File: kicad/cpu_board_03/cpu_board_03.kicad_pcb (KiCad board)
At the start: 2 copper layers, 99.1 x 94.2 mm, 60 parts, among them J1 DIN41612_02x32_AC, J10 PLD_aux, J11 Conn_01x09, J6 Conn_01x02_Socket, J9 Ram1 Enable, SW1 SW_Reset, SW2 SW_PWR, U1 W65C02SxP, U10 74HC245, U11 74HC245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

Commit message: update label names
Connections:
- net /~{CS_RAM0} renamed /~{RAM0_SEL}
- net /~{CS_RAM1} renamed /~{RAM1_SEL}
- net /~{CS_ROM} renamed /~{ROM_SEL}
- net /~{IO_RD_DIR} renamed /~{IO_RD}
- net /~{QOE} renamed /~{OE}
- net /~{QWE_RAM} renamed /~{QWE}
- net /~{SYS_CLK} renamed /~{IO_WR}

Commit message: update pcb
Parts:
- removed U14: 74AHC1G04, Package_TO_SOT_SMD:SOT-23-5_HandSoldering
- moved U13 3.14 mm to (113.5, 56.4)
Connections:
- U13 pad 1: Net-(U13-Pad1) -> /~{IO_WR}
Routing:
- net /CLOCK: track 55.8 -> 31.3 mm, vias 1 -> 0
- net Net-(U13-Pad1): track 17.4 -> 0.00 mm
- net VCC: track 546.1 -> 538.4 mm
- net /~{IO_WR}: track 51.9 -> 56.6 mm
- net Net-(U6-Cp): track 21.8 -> 18.3 mm
- net /~{IOEN_00_GPIO0}: track 112.8 -> 110.0 mm
- net GND: track 929.6 -> 928.8 mm, vias 76 -> 74

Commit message: cleaned up pullup mess
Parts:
- added D14: LED_Small, LED_SMD:LED_0805_2012Metric_Pad1.15x1.40mm_HandSolder, F.Cu at (46.5, 75.7)
- added R6: 10K, Resistor_SMD:R_0805_2012Metric_Pad1.20x1.40mm_HandSolder, F.Cu at (46.5, 73.2)
- added R7: 10K, Resistor_SMD:R_0805_2012Metric_Pad1.20x1.40mm_HandSolder, F.Cu at (46.5, 78.0)
- added R8: 10K, Resistor_SMD:R_0805_2012Metric_Pad1.20x1.40mm_HandSolder, F.Cu at (46.5, 65.5)
- moved C11 5.95 mm to (41.3, 61.2)
- moved R5 1.59 mm to (46.5, 70.6), turned to 0 degrees
- moved R3 0.55 mm to (46.5, 68.1), turned to 0 degrees
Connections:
- J1 pad a29: VCC -> /~{IRQ}
- J1 pad a30: /~{NMI} -> /BE
- J1 pad c29: GND -> /RDY
- J1 pad c30: /~{IRQ} -> /~{NMI}
- U1 pad 2: VCC -> /RDY
- U1 pad 36: VCC -> /BE
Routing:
- net /BE: track 0.00 -> 55.6 mm
- net /RDY: track 0.00 -> 34.3 mm
- net VCC: track 538.4 -> 512.2 mm, vias 4 -> 7
- net /~{IRQ}: track 41.1 -> 49.1 mm
- net /~{NMI}: track 57.6 -> 51.7 mm
- net Net-(D14-A): track 0.00 -> 2.30 mm
- net /RES: track 47.0 -> 47.9 mm
- net /~{RES}: track 74.3 -> 74.9 mm
- net GND: track 928.8 -> 928.2 mm, vias 74 -> 71
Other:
- board text added: "Rdy"

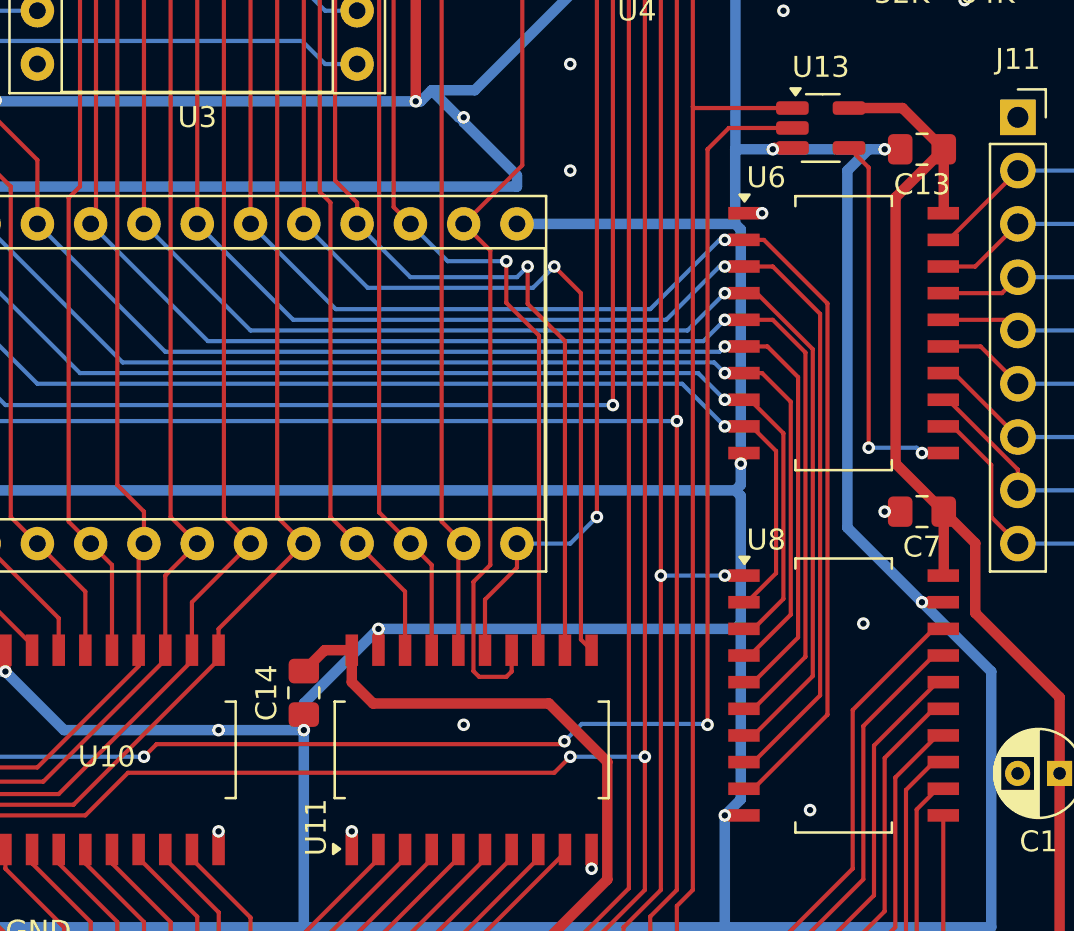
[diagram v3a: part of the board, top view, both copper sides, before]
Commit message: add bus tranceiver OE signal
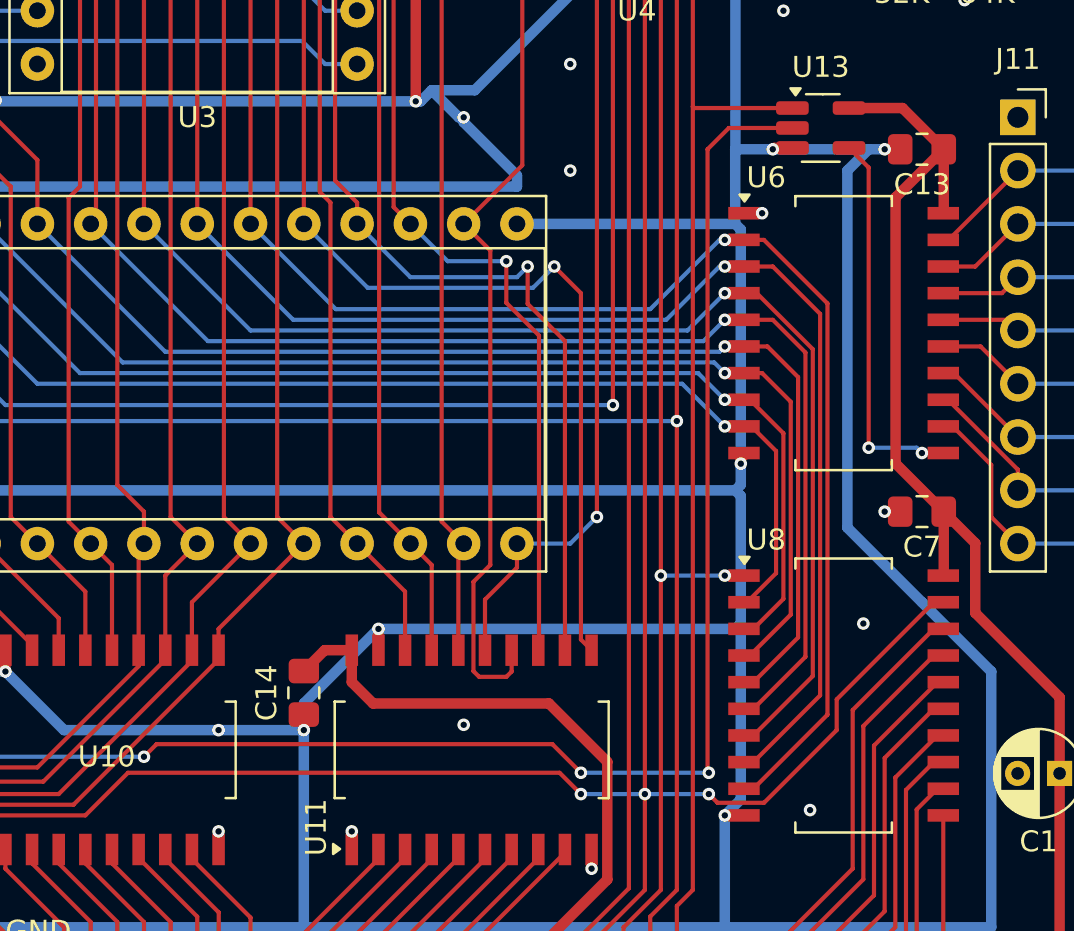
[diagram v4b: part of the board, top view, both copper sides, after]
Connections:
- U8 pad 19: GND -> /~{IO_SEL}
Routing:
- net /~{IO_SEL}: track 124.2 -> 143.5 mm, vias 5 -> 6
- net /~{IOEN_00_GPIO0}: track 110.0 -> 112.5 mm
- net GND: track 928.2 -> 927.2 mm, vias 71 -> 70
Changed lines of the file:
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@@
 			(size 1.5 0.6)
 			(layers "F.Cu" "F.Mask" "F.Paste")
-			(net 17 "GND")
+			(net 36 "/~{IO_SEL}")
 			(pinfunction "CE")
 			(pintype "input")
@@
 	)
 	(segment
-		(start 119.38 78.994)
-		(end 118.364 78.994)
-		(width 0.5)
-		(layer "F.Cu")
-		(net 17)
-	)
-	(segment
 		(start 109.728 72.136)
 		(end 109.88 71.984)
@@
 	)
 	(via
-		(at 118.364 78.994)
-		(size 0.6)
-		(drill 0.3)
-		(layers "F.Cu" "B.Cu")
-		(net 17)
-	)
-	(via
 		(at 34.798 65.024)
 		(size 0.6)
@@
 	)
 	(segment
+		(start 73.194 89.154)
+		(end 73.152 89.196)
+		(width 0.2)
+		(layer "F.Cu")
+		(net 36)
+	)
+	(segment
+		(start 110.837 88.553)
+		(end 108.619 88.553)
+		(width 0.2)
+		(layer "F.Cu")
+		(net 36)
+	)
+	(segment
 		(start 104.14 101.6)
 		(end 102.87 100.33)
@@
 	)
 	(segment
+		(start 108.619 88.553)
+		(end 108.204 88.138)
+		(width 0.2)
+		(layer "F.Cu")
+		(net 36)
+	)
+	(segment
 		(start 64.770948 91.948)
 		(end 64.77 91.947052)
@@
 	)
 	(segment
-		(start 105.156 42.164)
-		(end 109.22 38.1)
+		(start 118.93 78.994)
+		(end 114.3 83.624)
 		(width 0.2)
 		(layer "F.Cu")
@@
 	)
 	(segment
-		(start 78.486 89.154)
-		(end 73.194 89.154)
+		(start 80.518 87.122)
+		(end 78.486 89.154)
 		(width 0.2)
 		(layer "F.Cu")
@@
 	)
 	(segment
-		(start 101.6 86.36)
-		(end 100.838 87.122)
+		(start 105.156 42.164)
+		(end 109.22 38.1)
 		(width 0.2)
 		(layer "F.Cu")
@@
 	)
 	(segment
-		(start 100.838 87.122)
+		(start 102.108 88.138)
+		(end 101.092 87.122)
+		(width 0.2)
+		(layer "F.Cu")
+		(net 36)
+	)
+	(segment
+		(start 102.87 94.996)
+		(end 105.156 92.71)
+		(width 0.2)
+		(layer "F.Cu")
+		(net 36)
+	)
+	(segment
+		(start 114.3 83.624)
+		(end 114.3 85.09)
+		(width 0.2)
+		(layer "F.Cu")
+		(net 36)
+	)
+	(segment
+		(start 101.092 87.122)
 		(end 80.518 87.122)
 		(width 0.2)
@@
 	)
 	(segment
-		(start 80.518 87.122)
-		(end 78.486 89.154)
+		(start 119.38 78.994)
+		(end 118.93 78.994)
 		(width 0.2)
 		(layer "F.Cu")
@@
 	)
 	(segment
-		(start 102.87 94.996)
-		(end 105.156 92.71)
+		(start 78.486 89.154)
+		(end 73.194 89.154)
 		(width 0.2)
 		(layer "F.Cu")
@@
 	)
 	(segment
-		(start 102.87 100.33)
-		(end 102.87 94.996)
+		(start 114.3 85.09)
+		(end 110.837 88.553)
 		(width 0.2)
 		(layer "F.Cu")
@@
 	)
 	(segment
-		(start 105.156 92.71)
-		(end 105.156 42.164)
+		(start 102.87 100.33)
+		(end 102.87 94.996)
 		(width 0.2)
 		(layer "F.Cu")
@@
 	)
 	(segment
-		(start 73.194 89.154)
-		(end 73.152 89.196)
+		(start 105.156 92.71)
+		(end 105.156 42.164)
 		(width 0.2)
 		(layer "F.Cu")
@@
 	)
 	(via
-		(at 101.6 86.36)
+		(at 102.108 88.138)
 		(size 0.6)
 		(drill 0.3)
@@
 	)
 	(via
-		(at 105.156 86.36)
+		(at 105.156 88.138)
 		(size 0.6)
 		(drill 0.3)
@@
 		(net 36)
 	)
+	(via
+		(at 108.204 88.138)
+		(size 0.6)
+		(drill 0.3)
+		(layers "F.Cu" "B.Cu")
+		(net 36)
+	)
+	(segment
+		(start 105.156 88.138)
+		(end 108.204 88.138)
+		(width 0.2)
+		(layer "B.Cu")
+		(net 36)
+	)
+	(segment
+		(start 105.156 88.138)
+		(end 102.108 88.138)
+		(width 0.2)
+		(layer "B.Cu")
+		(net 36)
+	)
 	(segment
 		(start 64.770948 91.948)
@@
 	)
 	(segment
-		(start 105.156 86.36)
-		(end 101.6 86.36)
-		(width 0.2)
-		(layer "B.Cu")
-		(net 36)
-	)
-	(segment
 		(start 72.94 89.408)
 		(end 73.152 89.196)
@@
 	)
 	(segment
-		(start 112.188 56.388)
-		(end 109.16 56.388)
-		(width 0.2)
-		(layer "F.Cu")
-		(net 38)
-	)
-	(segment
 		(start 50.292 85.782)
 		(end 50.842 86.332)
@@
 	)
 	(segment
-		(start 108.144 57.404)
-		(end 108.144 84.836)
+		(start 108.204 87.122)
+		(end 108.144 87.062)
 		(width 0.2)
 		(layer "F.Cu")
@@
 	)
 	(segment
-		(start 50.842 94.234)
-		(end 52.07 95.462)
+		(start 102.108 87.122)
+		(end 100.745 85.759)
 		(width 0.2)
 		(layer "F.Cu")
@@
 	)
 	(segment
-		(start 81.881 85.759)
-		(end 101.185 85.759)
+		(start 100.745 85.759)
+		(end 81.881 85.759)
 		(width 0.2)
 		(layer "F.Cu")
@@
 	)
 	(segment
-		(start 58.24 84.656)
-		(end 50.543001 84.656)
+		(start 50.842 94.234)
+		(end 52.07 95.462)
 		(width 0.2)
 		(layer "F.Cu")
@@
 	)
 	(segment
-		(start 109.16 56.388)
-		(end 108.144 57.404)
+		(start 58.24 84.656)
+		(end 50.543001 84.656)
 		(width 0.2)
 		(layer "F.Cu")
@@
 	)
 	(segment
-		(start 81.28 86.36)
-		(end 81.881 85.759)
+		(start 108.144 57.404)
+		(end 109.16 56.388)
 		(width 0.2)
 		(layer "F.Cu")
@@
 	)
 	(segment
-		(start 101.185 85.759)
-		(end 101.323669 85.620331)
+		(start 108.144 87.062)
+		(end 108.144 57.404)
 		(width 0.2)
 		(layer "F.Cu")
@@
 	)
 	(segment
+		(start 81.881 85.759)
+		(end 81.28 86.36)
+		(width 0.2)
+		(layer "F.Cu")
+		(net 38)
+	)
+	(segment
 		(start 50.543001 84.656)
 		(end 50.292 84.907001)
@@
 		(net 38)
 	)
+	(segment
+		(start 109.16 56.388)
+		(end 112.188 56.388)
+		(width 0.2)
+		(layer "F.Cu")
+		(net 38)
+	)
 	(via
-		(at 101.323669 85.620331)
+		(at 102.108 87.122)
 		(size 0.6)
 		(drill 0.3)
@@
 	)
 	(via
-		(at 108.144 84.836)
+		(at 108.204 87.122)
 		(size 0.6)
 		(drill 0.3)
@@
 	)
 	(segment
-		(start 108.101 84.793)
-		(end 108.144 84.836)
-		(width 0.2)
-		(layer "B.Cu")
-		(net 38)
-	)
-	(segment
-		(start 101.323669 85.620331)
-		(end 102.151 84.793)
-		(width 0.2)
-		(layer "B.Cu")
-		(net 38)
-	)
-	(segment
-		(start 102.151 84.793)
-		(end 108.101 84.793)
+		(start 61.976 87.376)
+		(end 62.992 86.36)
 		(width 0.2)
 		(layer "B.Cu")
@@
 	)
 	(segment
-		(start 61.976 87.376)
-		(end 62.992 86.36)
+		(start 62.992 86.36)
+		(end 81.28 86.36)
 		(width 0.2)
 		(layer "B.Cu")
@@
 	)
 	(segment
-		(start 62.992 86.36)
-		(end 81.28 86.36)
+		(start 102.108 87.122)
+		(end 108.204 87.122)
 		(width 0.2)
 		(layer "B.Cu")

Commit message: route latest changes
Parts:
- removed J10: PLD_aux, Connector_PinHeader_2.54mm:PinHeader_1x03_P2.54mm_Vertical
- removed R8: 10K, Resistor_SMD:R_0805_2012Metric_Pad1.20x1.40mm_HandSolder
- removed U11: 74HC245, Package_SO:SO-20_12.8x7.5mm_P1.27mm
- removed U12: 74LS138, Package_SO:SO-16_3.9x9.9mm_P1.27mm
- added JP1: SolderJumper_3_Open, Jumper:SolderJumper-3_P1.3mm_Bridged12_RoundedPad1.0x1.5mm_NumberLabels, B.Cu at (93.2, 86.1)
- added JP2: SolderJumper_3_Open, Jumper:SolderJumper-3_P1.3mm_Bridged12_RoundedPad1.0x1.5mm_NumberLabels, B.Cu at (97.5, 86.1)
- moved C10 100.3 mm to (149.1, 74.9)
- moved C8 71.0 mm to (138.9, 98.6)
- moved R2 45.6 mm to (56.9, 85.6)
- moved D13 44.2 mm to (54.6, 85.6)
- moved U9 38.1 mm to (50.0, 86.4), turned to 90 degrees
- moved R1 27.1 mm to (42.4, 53.6), turned to 180 degrees
- moved C15 25.4 mm to (86.4, 82.6)
- moved U5 25.4 mm to (78.9, 88.6)
- moved SW1 25.2 mm to (43.4, 56.2)
- moved R3 19.7 mm to (62.5, 79.5)
- moved D14 19.5 mm to (62.2, 87.1), turned to -90 degrees
- moved C14 16.9 mm to (72.4, 86.8), turned to 90 degrees
- moved R7 15.9 mm to (59.4, 87.1), turned to -90 degrees
- moved U10 15.2 mm to (94.4, 86.3)
- moved R5 14.1 mm to (57.4, 79.5)
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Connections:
- J1 pad a11: /AB14 -> /~{IO_WR}
- J1 pad a12: /AB12 -> /AB4
- J1 pad a13: /AB10 -> /AB2
- J1 pad a14: /AB8 -> /AB0
- J1 pad a15: /AB6 -> VCC
- J1 pad a16: /AB4 -> /~{IOEN_06}
- J1 pad a17: /AB2 -> /~{IOEN_04}
- J1 pad a18: /AB0 -> /~{IOEN_02_UART}
- J1 pad a19: VCC -> /~{IOEN_00_GPIO0}
- J1 pad a21: /~{IOEN_14} -> /~{NMI}
- J1 pad a22: /~{IOEN_12} -> /RDY
- J1 pad a23: /~{IOEN_10} -> unconnected-(J1-Pin_a23-Pada23)
- J1 pad a24: /~{IOEN_08} -> unconnected-(J1-Pin_a24-Pada24)
- J1 pad a25: /~{IOEN_06} -> unconnected-(J1-Pin_a25-Pada25)
- J1 pad a26: /~{IOEN_04} -> unconnected-(J1-Pin_a26-Pada26)
- J1 pad a27: /~{IOEN_02_UART} -> unconnected-(J1-Pin_a27-Pada27)
- J1 pad a28: /~{IOEN_00_GPIO0} -> unconnected-(J1-Pin_a28-Pada28)
- J1 pad a29: /~{IRQ} -> unconnected-(J1-Pin_a29-Pada29)
- J1 pad a30: /BE -> unconnected-(J1-Pin_a30-Pada30)
- J1 pad a7: /SYS_CLK -> /CLOCK
- J1 pad a8: /~{IO_SEL} -> /PLD_O8
- J1 pad c11: /AB15 -> /~{IO_SEL_BUS}
- J1 pad c12: /AB13 -> /~{IO_RD}
- J1 pad c13: /AB11 -> /AB3
- J1 pad c14: /AB9 -> /AB1
- J1 pad c15: /AB7 -> GND
- J1 pad c16: /AB5 -> /~{IOEN_07}
- J1 pad c17: /AB3 -> /~{IOEN_05}
- J1 pad c18: /AB1 -> /~{IOEN_03}
- J1 pad c19: GND -> /~{IOEN_01}
- J1 pad c21: /~{IOEN_15} -> /SYNC
- J1 pad c22: /~{IOEN_13} -> /~{IRQ}
- J1 pad c23: /~{IOEN_11} -> unconnected-(J1-Pin_c23-Padc23)
- J1 pad c24: /~{IOEN_09} -> unconnected-(J1-Pin_c24-Padc24)
- J1 pad c25: /~{IOEN_07} -> unconnected-(J1-Pin_c25-Padc25)
- J1 pad c26: /~{IOEN_05} -> unconnected-(J1-Pin_c26-Padc26)
- J1 pad c27: /~{IOEN_03} -> unconnected-(J1-Pin_c27-Padc27)
- J1 pad c28: /~{IOEN_01} -> unconnected-(J1-Pin_c28-Padc28)
- J1 pad c29: /RDY -> unconnected-(J1-Pin_c29-Padc29)
- J1 pad c30: /~{NMI} -> unconnected-(J1-Pin_c30-Padc30)
- J1 pad c7: /~{IO_WR} -> /PLD_O9
- J1 pad c8: /~{IO_RD} -> /PLD_O7
- J1 pad c9: /PLD_O0 -> /PLD_I1
- U1 pad 36: /BE -> unconnected-(U1-BE-Pad36)
- U1 pad 7: unconnected-(U1-SYNC-Pad7) -> /SYNC
- U10 pad 11: /A7 -> /~{IO_SEL}
- U10 pad 12: /A6 -> Net-(JP2-C)
- U10 pad 13: /A5 -> Net-(JP1-C)
- U10 pad 7: /AB5 -> /~{IO_RD}
- U10 pad 8: /AB6 -> /~{IO_WR}
- U10 pad 9: /AB7 -> /~{IO_SEL_BUS}
- U13 pad 1: /~{IO_WR} -> /~{IOEN_00_GPIO0}
- U13 pad 2: /~{IOEN_00_GPIO0} -> /~{IO_WR}
- U4 pad 14: /~{IO_WR} -> /PLD_O9
- U4 pad 15: /SYS_CLK -> /PLD_O8
- U4 pad 16: /~{IO_RD} -> /PLD_O7
- U4 pad 23: /PLD_O0 -> /SYS_CLK
- U5 pad 1: /A4 -> /A5
- U5 pad 2: /A5 -> /A6
- U5 pad 3: /A6 -> /A7
- U5 pad 5: /A7 -> GND
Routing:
- net VCC: track 512.2 -> 383.4 mm, vias 7 -> 0
- net GND: track 927.2 -> 828.3 mm, vias 70 -> 68
- net /CLOCK: track 31.3 -> 127.4 mm, vias 0 -> 2
- net /PLD_O0: track 78.7 -> 0.00 mm
- net /PLD_O7: track 0.00 -> 72.6 mm, vias 0 -> 3
- net /~{OE}: track 55.8 -> 127.9 mm, vias 1 -> 4
- net /~{QWE}: track 74.3 -> 146.1 mm, vias 1 -> 4
- net /PLD_O8: track 0.00 -> 70.8 mm, vias 0 -> 3
- net /~{IO_SEL}: track 143.5 -> 81.5 mm, vias 6 -> 3
- net /PLD_I1: track 11.1 -> 73.0 mm
- net /BE: track 55.6 -> 0.00 mm
- net /PLD_O9: track 0.00 -> 51.9 mm
- net /~{IOEN_00_GPIO0}: track 112.5 -> 78.7 mm
- net /A15: track 92.2 -> 59.5 mm, vias 2 -> 1
- net /RES: track 47.9 -> 15.3 mm
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
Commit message: finished basic routing
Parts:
- added J2: Clock, Connector_PinSocket_2.54mm:PinSocket_1x02_P2.54mm_Vertical, F.Cu at (127.5, 33.0)
- moved C8 93.9 mm to (46.4, 82.7), turned to 90 degrees
- moved C10 28.2 mm to (126.1, 91.2), turned to 0 degrees
- moved C12 2.41 mm to (127.8, 27.2)
- turned C15 to -90 degrees
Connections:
- J1 pad a7: /CLOCK -> unconnected-(J1-Pin_a7-Pada7)
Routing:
- net VCC: track 383.4 -> 488.8 mm, vias 0 -> 8
- net /CLOCK: track 127.4 -> 36.4 mm, vias 2 -> 0
- net GND: track 828.3 -> 835.2 mm, vias 68 -> 70
- net /~{IO_SEL}: track 81.5 -> 79.4 mm, vias 3 -> 2
- net /A5: track 97.1 -> 96.1 mm
- net /A6: track 101.9 -> 100.9 mm

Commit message: finished drc errors
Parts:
- removed C15: 100nF, Capacitor_SMD:C_0805_2012Metric_Pad1.18x1.45mm_HandSolder
- added JP3: SolderJumper_3_Open, Jumper:SolderJumper-3_P1.3mm_Open_RoundedPad1.0x1.5mm, B.Cu at (85.3, 89.6)
- JP1, JP2: footprint Jumper:SolderJumper-3_P1.3mm_Bridged12_RoundedPad1.0x1.5mm_NumberLabels -> Jumper:SolderJumper-3_P1.3mm_Open_RoundedPad1.0x1.5mm
- moved C10 40.7 mm to (86.4, 82.6), turned to -90 degrees
- moved C14 1.96 mm to (72.4, 84.9)
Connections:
- U5 pad 5: GND -> Net-(JP3-C)
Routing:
- net /~{IO_SEL}: track 79.4 -> 115.0 mm, vias 2 -> 4
- net GND: track 835.2 -> 851.3 mm, vias 70 -> 71
- net /A4: track 90.2 -> 105.1 mm, vias 0 -> 1
- net VCC: track 488.8 -> 502.6 mm
- net Net-(JP3-C): track 0.00 -> 7.08 mm, vias 0 -> 1
- net Net-(D14-A): track 0.00 -> 2.80 mm
- net Net-(D13-A): track 0.00 -> 2.30 mm
- net /~{OE}: track 127.9 -> 125.7 mm, vias 4 -> 2
- net /~{QWE}: track 146.1 -> 144.6 mm, vias 4 -> 2

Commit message: updated routing & semi-final checks
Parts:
- moved SW1 25.8 mm to (43.4, 30.5)
- moved R1 13.7 mm to (42.4, 39.9)
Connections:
- J1 pad a20: unconnected-(J1-Pin_a20-Pada20) -> VCC
- J1 pad c20: unconnected-(J1-Pin_c20-Padc20) -> GND
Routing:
- net Net-(U9-~{PB_RST}): track 37.3 -> 60.4 mm
- net /SYS_CLK: track 133.8 -> 124.1 mm
- net VCC: track 502.6 -> 512.2 mm
- net GND: track 851.3 -> 847.7 mm, vias 71 -> 78
- net Net-(JP1-C): track 6.81 -> 8.99 mm, vias 1 -> 3
- net /~{RES}: track 54.7 -> 55.9 mm, vias 0 -> 2
- net /RDY: track 36.4 -> 35.2 mm
- net /A7: track 105.8 -> 104.6 mm
- net /~{IO_SEL}: track 115.0 -> 116.0 mm
- net /A6: track 100.9 -> 100.2 mm
- net /~{OE}: track 125.7 -> 125.0 mm, vias 2 -> 4
- net /PLD_O7: track 72.8 -> 72.2 mm
- net /~{QWE}: track 144.6 -> 145.0 mm, vias 2 -> 4
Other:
- board text added: "Addr"
- board text added: "Ctl"
- board text added: "Irq/Stat"
- board text added: "PLD"
- board text added: "RDY"
- board text added: "Reset"
- board text removed: "Addressbus"
- board text removed: "PLD I/O"
- board text removed: "Reset/Irq"
